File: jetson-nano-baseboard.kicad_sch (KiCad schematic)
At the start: 3 parts

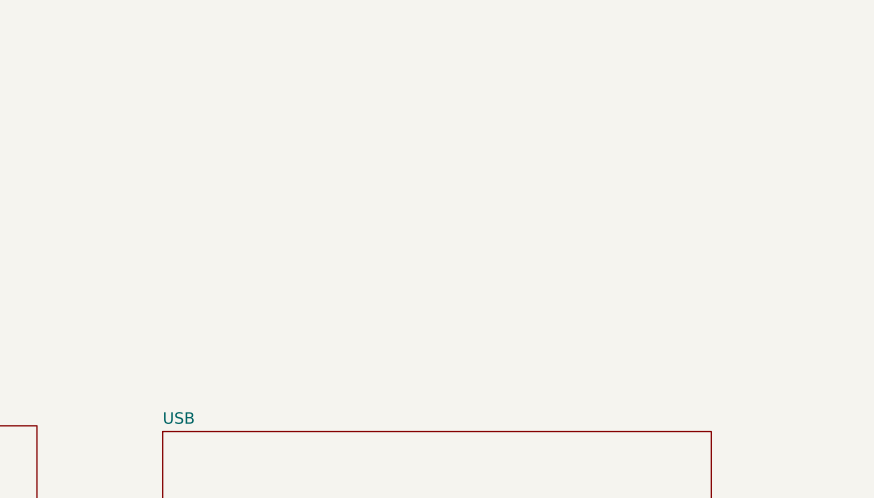
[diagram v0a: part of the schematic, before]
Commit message: WIP: Re-design base board
1. change to more common connector from JLC
2. add WIFI M.2 Key-E connector
3. add USB Hub which contained in nVidia version board
4. change DC connecotor to XT30
5. change USB Mico-B to USB Type C
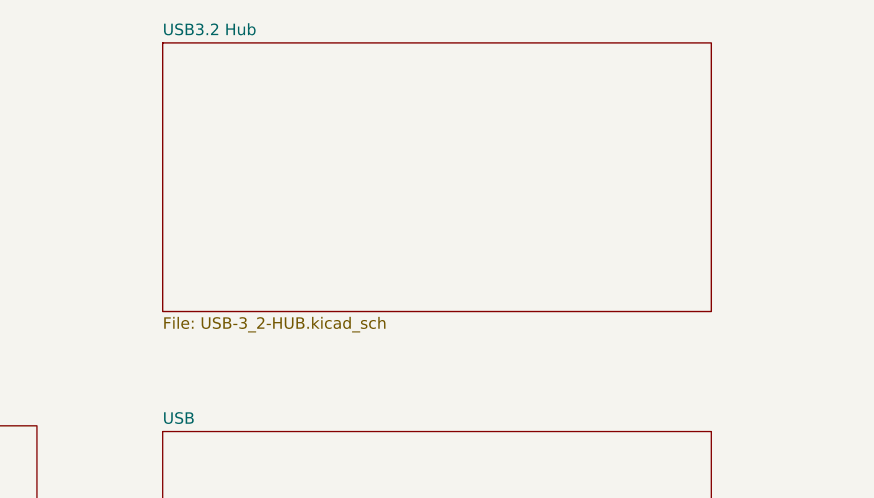
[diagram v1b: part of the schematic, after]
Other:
- added sheet USB3.2 Hub (USB-3_2-HUB.kicad_sch)
